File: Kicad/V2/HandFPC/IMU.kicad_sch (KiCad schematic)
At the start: 4 parts, among them U2 ICM-42688-P_I2C

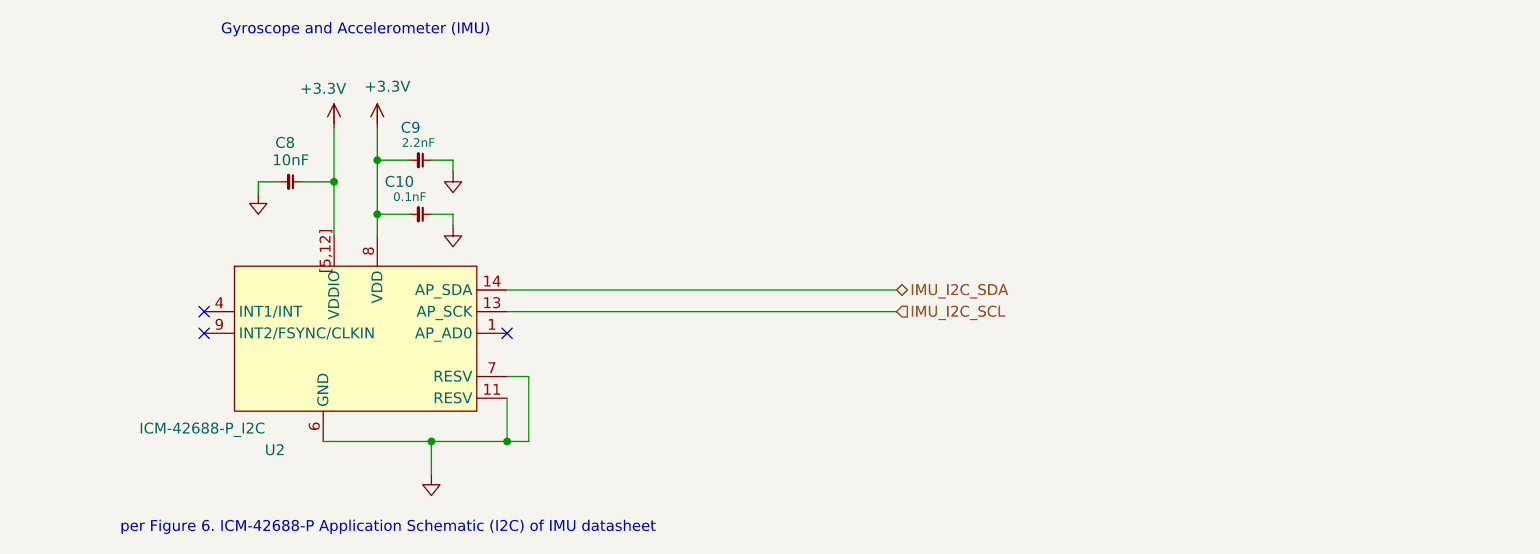
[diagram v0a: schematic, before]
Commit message: hand FPC pass erc no warning no error
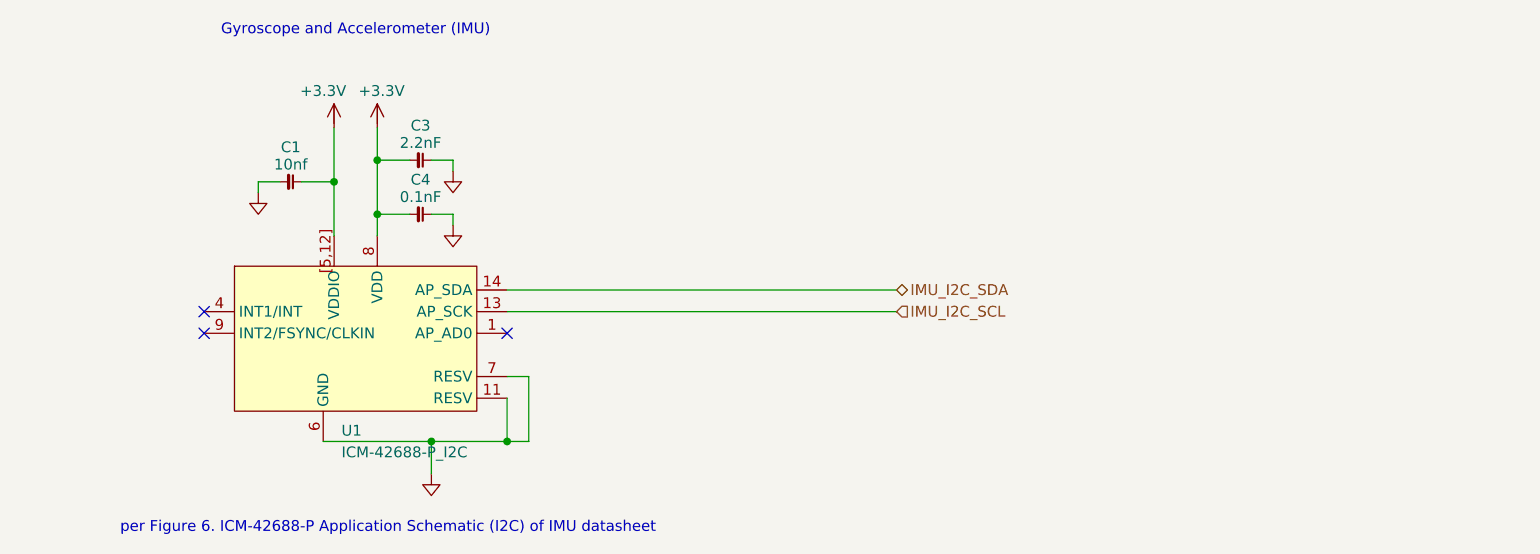
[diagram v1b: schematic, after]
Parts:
- removed C10: 0.1nF, MyGlove:Capacitor_0603, symbol G-Love:C
- removed C8: 10nF, MyGlove:Capacitor_0603, symbol G-Love:C
- removed C9: 2.2nF, MyGlove:Capacitor_0603, symbol G-Love:C
- removed U2: ICM-42688-P_I2C, MyGlove:ICM-42688-P, symbol G-Love:ICM-42688-P_I2C
- added C1: 10nf, symbol G-Love-Symbols:C
- added C3: 2.2nF, symbol G-Love-Symbols:C
- added C4: 0.1nF, symbol G-Love-Symbols:C
- added U1: ICM-42688-P_I2C, symbol G-Love-Symbols:ICM-42688-P_I2C
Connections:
- net +3.3V: now also C1.2, C3.1, C4.1, U1.8 (VDD), U1.[5,12] (VDDIO)
- net GND: now also C1.1, C3.2, C4.2, U1.11 (RESV), U1.6 (GND), U1.7 (RESV)
- net IMU_I2C_SCL: now also U1.13 (AP_SCK)
- net IMU_I2C_SDA: now also U1.14 (AP_SDA)

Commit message: add custom symbol for FPC connector
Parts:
- renumbered C3 to C2, C4 to C3
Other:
- note added: "Level Shifter to 5V"
- note added: "On WristBoard"
- note added: "Pullup 10k"
- note added: "SCL"
- note added: "SDA"
- note added: "VCC"
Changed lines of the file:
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@@
 	(generator_version "10.0")
 	(paper "A4")
+	(rectangle
+		(start 166.624 58.166)
+		(end 184.15 64.262)
+		(stroke
+			(width 0)
+			(type default)
+		)
+		(fill
+			(type none)
+		)
+	)
+	(rectangle
+		(start 163.576 70.866)
+		(end 161.036 66.802)
+		(stroke
+			(width 0)
+			(type default)
+		)
+		(fill
+			(type none)
+		)
+	)
+	(rectangle
+		(start 161.036 50.8)
+		(end 163.576 54.864)
+		(stroke
+			(width 0)
+			(type default)
+		)
+		(fill
+			(type none)
+		)
+	)
 	(text "Gyroscope and Accelerometer (IMU)\n"
 		(exclude_from_sim no)
@@
 		)
 	)
+	(text "SDA"
+		(exclude_from_sim no)
+		(at 193.04 59.69 0)
+		(effects
+			(font
+				(size 1.27 1.27)
+			)
+		)
+	)
+	(text "SCL\n"
+		(exclude_from_sim no)
+		(at 193.294 62.23 0)
+		(effects
+			(font
+				(size 1.27 1.27)
+			)
+		)
+	)
+	(text "VCC"
+		(exclude_from_sim no)
+		(at 162.56 77.978 0)
+		(effects
+			(font
+				(size 1.27 1.27)
+			)
+		)
+	)
+	(text "Level Shifter \nto 5V"
+		(exclude_from_sim no)
+		(at 175.514 61.214 0)
+		(effects
+			(font
+				(size 1.27 1.27)
+			)
+		)
+	)
+	(text "VCC"
+		(exclude_from_sim no)
+		(at 162.052 43.688 0)
+		(effects
+			(font
+				(size 1.27 1.27)
+			)
+		)
+	)
+	(text "Pullup 10k\n"
+		(exclude_from_sim no)
+		(at 169.926 52.07 0)
+		(effects
+			(font
+				(size 1.27 1.27)
+			)
+		)
+	)
+	(text "On WristBoard"
+		(exclude_from_sim no)
+		(at 193.294 33.782 0)
+		(effects
+			(font
+				(size 1.27 1.27)
+			)
+		)
+	)
 	(text "per Figure 6. ICM-42688-P Application Schematic (I2C) of IMU datasheet"
 		(exclude_from_sim no)
@@
 		)
 	)
+	(text "Pullup 10k\n"
+		(exclude_from_sim no)
+		(at 169.926 69.088 0)
+		(effects
+			(font
+				(size 1.27 1.27)
+			)
+		)
+	)
 	(junction
 		(at 82.55 77.47)
@@
 		)
 	)
+	(polyline
+		(pts
+			(xy 162.306 75.438) (xy 162.306 71.12)
+		)
+		(stroke
+			(width 0)
+			(type default)
+		)
+	)
 	(wire
 		(pts
@@
 		)
 	)
+	(polyline
+		(pts
+			(xy 184.15 62.484) (xy 190.754 62.484)
+		)
+		(stroke
+			(width 0)
+			(type default)
+		)
+	)
 	(wire
 		(pts
@@
 		)
 	)
+	(polyline
+		(pts
+			(xy 184.15 59.69) (xy 190.246 59.69)
+		)
+		(stroke
+			(width 0)
+			(type default)
+		)
+	)
 	(wire
 		(pts
@@
 		)
 	)
+	(polyline
+		(pts
+			(xy 162.306 55.118) (xy 162.306 59.436)
+		)
+		(stroke
+			(width 0)
+			(type default)
+		)
+	)
 	(wire
 		(pts
@@
 		)
 	)
+	(polyline
+		(pts
+			(xy 143.51 59.69) (xy 166.37 59.69)
+		)
+		(stroke
+			(width 0)
+			(type default)
+		)
+	)
 	(wire
 		(pts
@@
 		)
 	)
+	(polyline
+		(pts
+			(xy 162.306 66.548) (xy 162.306 62.23)
+		)
+		(stroke
+			(width 0)
+			(type default)
+		)
+	)
+	(polyline
+		(pts
+			(xy 162.306 46.228) (xy 162.306 50.546)
+		)
+		(stroke
+			(width 0)
+			(type default)
+		)
+	)
 	(wire
 		(pts
 			(xy 73.66 77.47) (xy 82.55 77.47)
+		)
+		(stroke
+			(width 0)
+			(type default)
+		)
+	)
+	(polyline
+		(pts
+			(xy 143.51 61.976) (xy 166.116 61.976)
 		)
 		(stroke
@@
 		)
 	)
+	(rule_area
+		(exclude_from_sim no)
+		(in_bom yes)
+		(on_board yes)
+		(dnp no)
+		(polyline
+			(pts
+				(xy 144.78 35.56) (xy 200.66 35.56) (xy 200.914 88.9) (xy 144.78 88.9)
+			)
+			(stroke
+				(width 0)
+				(type dash)
+				(color 255 255 194 1)
+			)
+			(fill
+				(type none)
+			)
+		)
+	)
 	(symbol
 		(lib_id "G-Love-Symbols:C")
@@
 		(in_pos_files yes)
 		(dnp no)
-		(property "Reference" "C3"
+		(property "Reference" "C2"
 			(at 72.39 40.386 90)
 			(show_name no)
@@
 			(project "HandFPC"
 				(path "/7221f3d8-f3bc-4a50-a6fd-69c2d8ca27db/f73c6c7b-472d-4c5d-b434-31d2ac317fba"
-					(reference "C3")
+					(reference "C2")
 					(unit 1)
 				)
@@
 		(dnp no)
 		(fields_autoplaced yes)
-		(property "Reference" "GND010"
+		(property "Reference" "GND011"
 			(at 76.2 55.626 0)
 			(hide yes)
@@
 			(project "HandFPC"
 				(path "/7221f3d8-f3bc-4a50-a6fd-69c2d8ca27db/f73c6c7b-472d-4c5d-b434-31d2ac317fba"
-					(reference "GND010")
+					(reference "GND011")
 					(unit 1)
 				)
@@
 		(in_pos_files yes)
 		(dnp no)
-		(property "Reference" "#PWR06"
+		(property "Reference" "#PWR014"
 			(at 66.04 41.148 0)
 			(hide yes)
@@
 			(project "HandFPC"
 				(path "/7221f3d8-f3bc-4a50-a6fd-69c2d8ca27db/f73c6c7b-472d-4c5d-b434-31d2ac317fba"
-					(reference "#PWR06")
+					(reference "#PWR014")
 					(unit 1)
 				)
@@
 		(dnp no)
 		(fields_autoplaced yes)
-		(property "Reference" "GND07"
+		(property "Reference" "GND010"
 			(at 76.2 49.276 0)
 			(hide yes)
@@
 			(project "HandFPC"
 				(path "/7221f3d8-f3bc-4a50-a6fd-69c2d8ca27db/f73c6c7b-472d-4c5d-b434-31d2ac317fba"
-					(reference "GND07")
+					(reference "GND010")
 					(unit 1)
 				)
@@
 		(in_pos_files yes)
 		(dnp no)
-		(property "Reference" "C4"
+		(property "Reference" "C3"
 			(at 72.39 46.736 90)
 			(show_name no)
@@
 			(project "HandFPC"
 				(path "/7221f3d8-f3bc-4a50-a6fd-69c2d8ca27db/f73c6c7b-472d-4c5d-b434-31d2ac317fba"
-					(reference "C4")
+					(reference "C3")
 					(unit 1)
 				)
@@
 		(in_pos_files yes)
 		(dnp no)
-		(property "Reference" "#PWR08"
+		(property "Reference" "#PWR015"
 			(at 71.12 41.148 0)
 			(hide yes)
@@
 			(project "HandFPC"
 				(path "/7221f3d8-f3bc-4a50-a6fd-69c2d8ca27db/f73c6c7b-472d-4c5d-b434-31d2ac317fba"
-					(reference "#PWR08")
+					(reference "#PWR015")
 					(unit 1)
 				)

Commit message: fix flex sensor mixed up with force sensor
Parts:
- C1, C2, C3: footprint (none) -> MyGlove:Capacitor_0603
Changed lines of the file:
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@@
 			)
 		)
-		(property "Footprint" ""
+		(property "Footprint" "MyGlove:Capacitor_0603"
 			(at 57.15 46.99 0)
 			(hide yes)
@@
 			)
 		)
-		(property "Footprint" ""
+		(property "Footprint" "MyGlove:Capacitor_0603"
 			(at 72.39 44.45 0)
 			(hide yes)
@@
 			)
 		)
-		(property "Footprint" ""
+		(property "Footprint" "MyGlove:Capacitor_0603"
 			(at 72.39 50.8 0)
 			(hide yes)

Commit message: add FPC footprints
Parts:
- C1, C2, C3: footprint MyGlove:Capacitor_0603 -> MyGlove:FPC_0603
- U1: footprint (none) -> MyGlove:FPC_ICM-42688-P
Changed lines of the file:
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@@
 			)
 		)
-		(property "Footprint" "MyGlove:Capacitor_0603"
+		(property "Footprint" "MyGlove:FPC_0603"
 			(at 57.15 46.99 0)
 			(hide yes)
@@
 			)
 		)
-		(property "Footprint" "MyGlove:Capacitor_0603"
+		(property "Footprint" "MyGlove:FPC_0603"
 			(at 72.39 44.45 0)
 			(hide yes)
@@
 			)
 		)
-		(property "Footprint" ""
+		(property "Footprint" "MyGlove:FPC_ICM-42688-P"
 			(at 64.77 66.04 0)
 			(hide yes)
@@
 			)
 		)
-		(property "Footprint" "MyGlove:Capacitor_0603"
+		(property "Footprint" "MyGlove:FPC_0603"
 			(at 72.39 50.8 0)
 			(hide yes)

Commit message: add routing
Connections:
- net GND: now also U1.1 (AP_AD0)
- no-connect marks 3 -> 2
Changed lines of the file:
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@@
-	)
-	(no_connect
-		(at 82.55 64.77)
 	)
 	(no_connect
@@
 	(wire
 		(pts
+			(xy 88.9 64.77) (xy 88.9 69.85)
+		)
+		(stroke
+			(width 0)
+			(type default)
+		)
+	)
+	(wire
+		(pts
 			(xy 76.2 52.07) (xy 76.2 50.8)
 		)
@@
 		(pts
 			(xy 62.23 40.64) (xy 62.23 46.99)
+		)
+		(stroke
+			(width 0)
+			(type default)
+		)
+	)
+	(wire
+		(pts
+			(xy 82.55 64.77) (xy 88.9 64.77)
 		)
 		(stroke
@@
 					(unit 1)
 				)
+			)
+		)
+	)
+	(symbol
+		(lib_id "G-Love-Symbols:GND")
+		(at 88.9 69.85 0)
+		(unit 1)
+		(body_style 1)
+		(exclude_from_sim no)
+		(in_bom no)
+		(on_board no)
+		(in_pos_files yes)
+		(dnp no)
+		(fields_autoplaced yes)
+		(property "Reference" "GND017"
+			(at 88.9 73.406 0)
+			(hide yes)
+			(show_name no)
+			(do_not_autoplace no)
+			(effects
+				(font
+					(size 1.27 1.27)
+				)
+			)
+		)
+		(property "Value" "GND"
+			(at 88.9 73.406 0)
+			(hide yes)
+			(show_name no)
+			(do_not_autoplace no)
+			(effects
+				(font
+					(size 1.27 1.27)
+				)
+			)
+		)
+		(property "Footprint" ""
+			(at 88.9 69.85 0)
+			(hide yes)
+			(show_name no)
+			(do_not_autoplace no)
+			(effects
+				(font
+					(size 1.27 1.27)
+				)
+			)
+		)
+		(property "Datasheet" ""
+			(at 88.9 69.85 0)
+			(hide yes)
+			(show_name no)
+			(do_not_autoplace no)
+			(effects
+				(font
+					(size 1.27 1.27)
+				)
+			)
+		)
+		(property "Description" ""
+			(at 88.9 69.85 0)
+			(hide yes)
+			(show_name no)
+			(do_not_autoplace no)
+			(effects
+				(font
+					(size 1.27 1.27)
+				)
+			)
+		)
+		(pin "1"
+		)
+		(instances
+			(project "HandFPC"
+				(path "/7221f3d8-f3bc-4a50-a6fd-69c2d8ca27db/f73c6c7b-472d-4c5d-b434-31d2ac317fba"
+					(reference "GND017")
+					(unit 1)
+				)
